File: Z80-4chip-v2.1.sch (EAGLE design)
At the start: 100 parts, among them IC1 Z84C00xx (-Z80-), IC2 CXK581000 (128k * 8), IC4 7400N, M1 WIRE-VIA8, U1 ATMEGA32A-PU

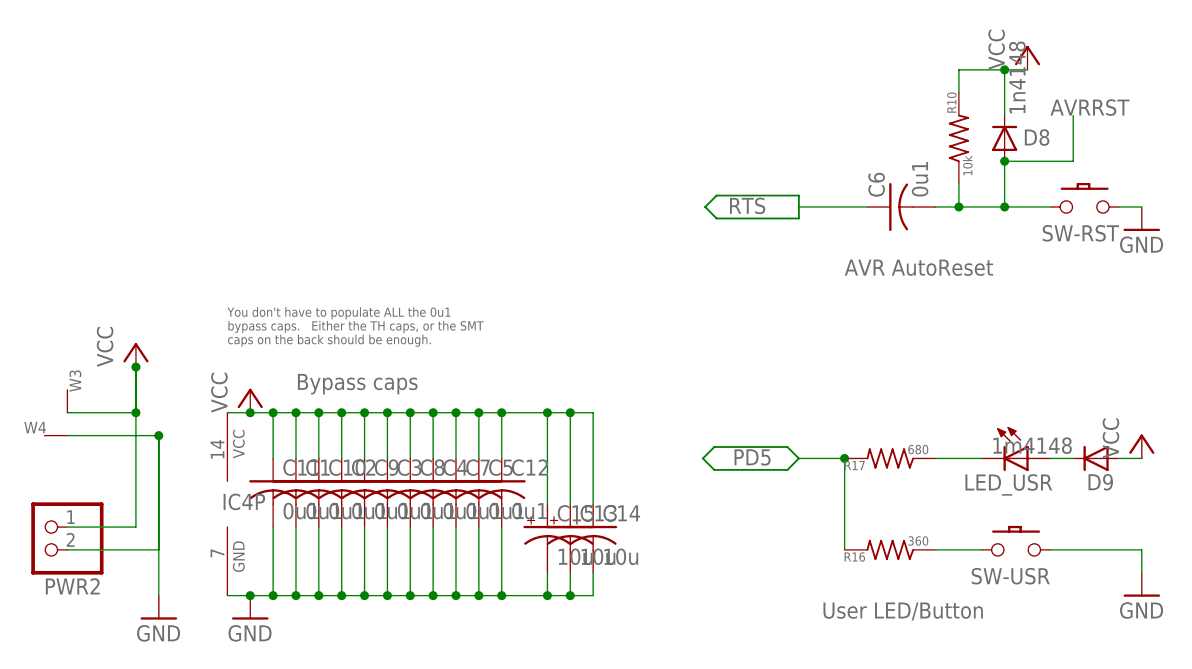
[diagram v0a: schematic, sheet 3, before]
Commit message: Add VCC/GND labels to bottom silk for new prototype-area vias. Bump version to V2.1 to account for the new power vias in prototype area. rename files to reflect version number (Z80-4chip-v2.1.*) Add zip of v2.1 gerbers to Gerbers-V2 directory.
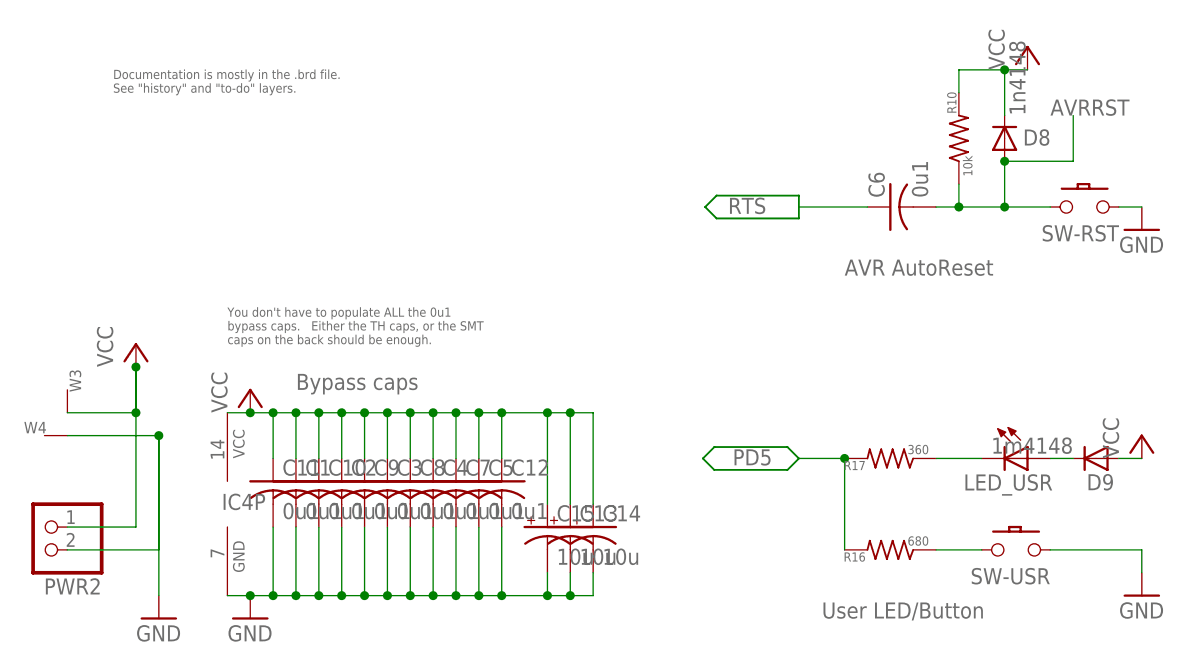
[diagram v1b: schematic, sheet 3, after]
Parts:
- R16: value 360 -> 680
- R17: value 680 -> 360
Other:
- note added: "Documentation is mostly in the .brd file. See "history" and "to-do" layers."
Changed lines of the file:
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@@
 <part name="GND10" library="supply1" deviceset="GND" device=""/>
 <part name="GND11" library="supply1" deviceset="GND" device=""/>
-<part name="R16" library="my-rcl" deviceset="R-US_" device="0207/07V" value="360"/>
-<part name="R17" library="my-rcl" deviceset="R-US_" device="0207/07V" value="680"/>
+<part name="R16" library="my-rcl" deviceset="R-US_" device="0207/07V" value="680"/>
+<part name="R17" library="my-rcl" deviceset="R-US_" device="0207/07V" value="360"/>
 <part name="P+9" library="supply1" deviceset="VCC" device=""/>
 <part name="D9" library="mylib4" deviceset="DIODE-SIGNAL" device="-5" value="1m4148"/>
@@
 <text x="91.44" y="-50.8" size="1.778" layer="97" ratio="10">Wait State
 Flip Flop</text>
+<text x="-88.9" y="66.04" size="1.016" layer="95">Documentation is mostly in the .brd file.
+See "history" and "to-do" layers.</text>
 </plain>
 <instances>
@@
 <text x="73.66" y="-38.1" size="1.778" layer="97" ratio="10" rot="R180">Boot</text>
 <text x="176.276" y="41.656" size="1.778" layer="97" ratio="10" rot="R270">Serial</text>
+<text x="-7.62" y="-22.86" size="1.016" layer="95">Documentation is mostly in the .brd file.
+See "history" and "to-do" layers.</text>
 </plain>
 <instances>
@@
 <text x="76.2" y="86.36" size="1.778" layer="96">AVR AutoReset</text>
 <text x="73.66" y="48.26" size="1.778" layer="96">User LED/Button</text>
+<text x="-5.08" y="106.68" size="1.016" layer="95">Documentation is mostly in the .brd file.
+See "history" and "to-do" layers.</text>
 </plain>
 <instances>
